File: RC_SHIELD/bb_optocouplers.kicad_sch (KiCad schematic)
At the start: 40 parts, among them U1 SFH6345, U2 SFH6345, U6 SFH6345, U8 SFH6345

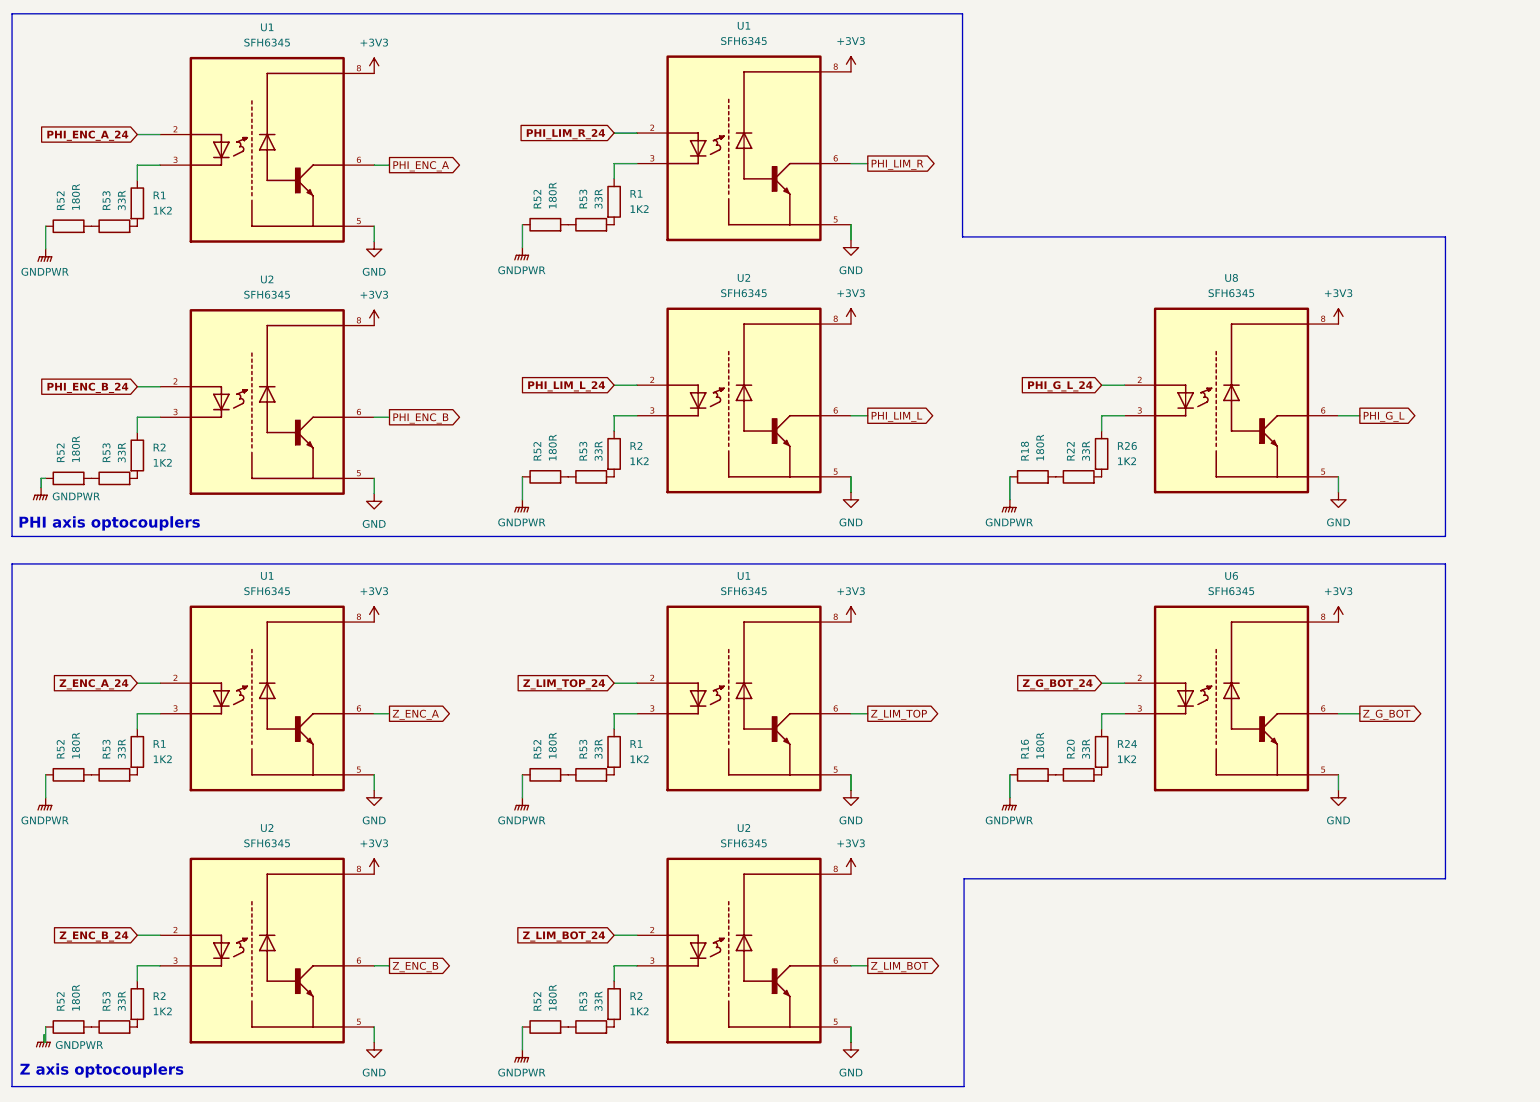
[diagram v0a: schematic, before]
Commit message: Revert "[SCH] reorganized optocouplers and tidied up page 2"
This reverts commit 005640e4067293c5014d1b79d289b32d97da3ff9.
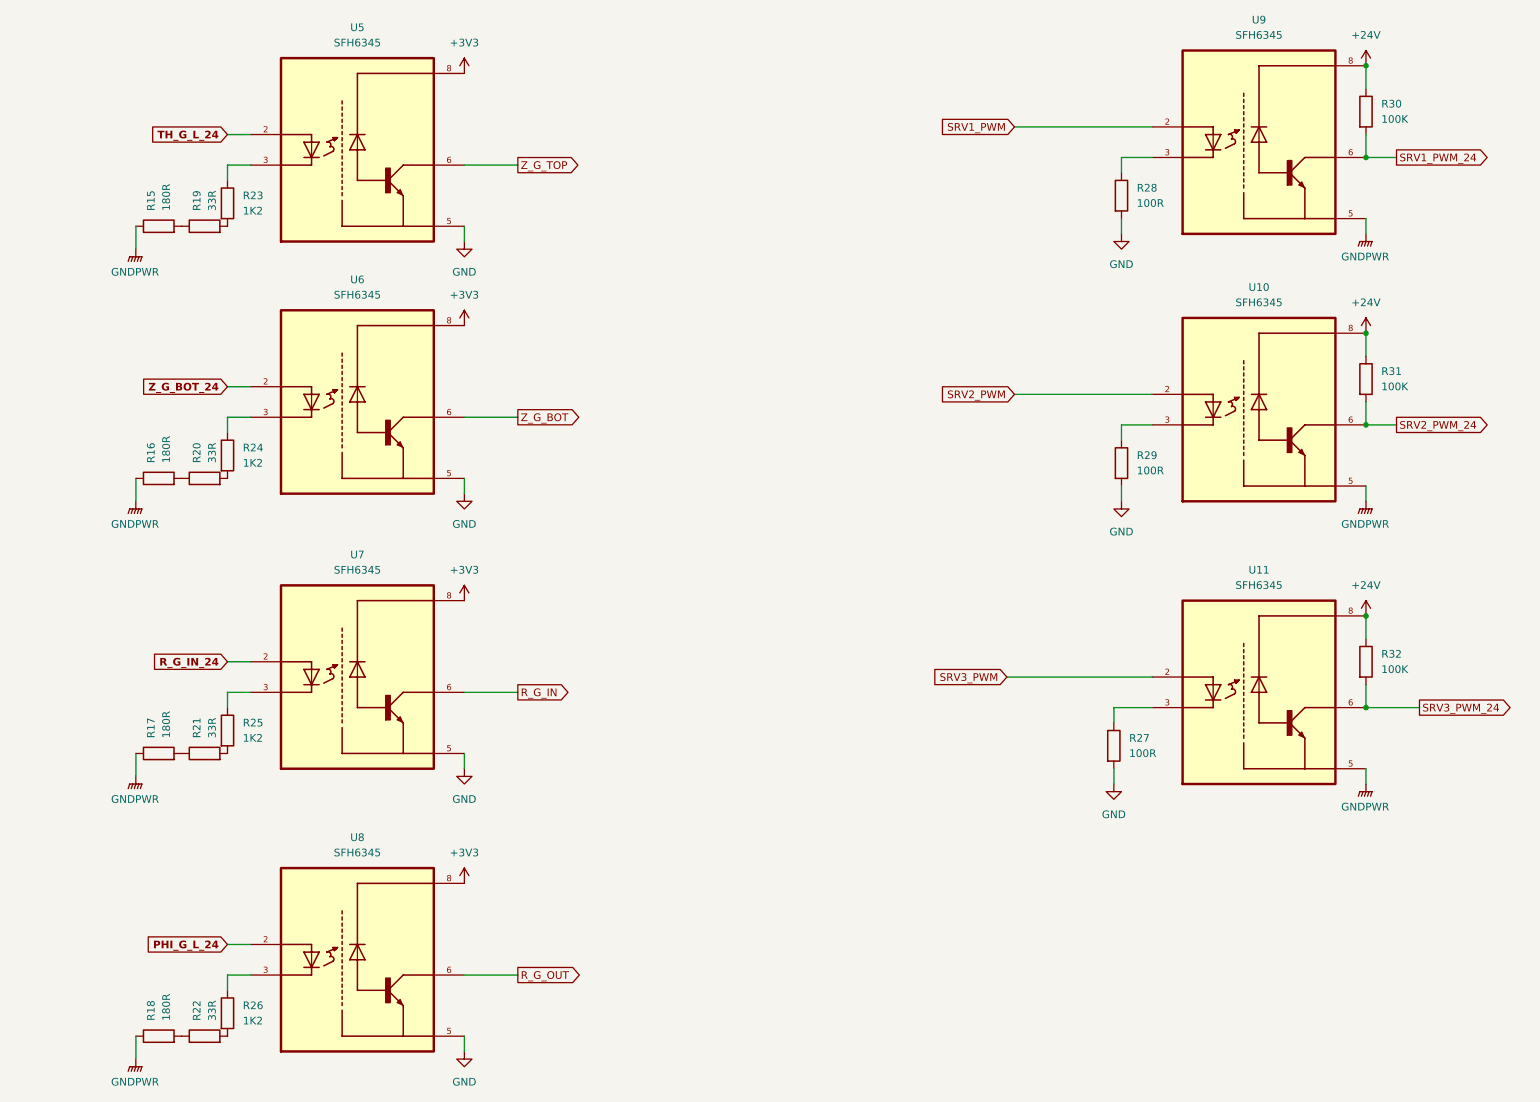
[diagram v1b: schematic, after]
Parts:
- removed R1 (x4), R2 (x4): 1K2, Resistor_SMD:R_0805_2012Metric_Pad1.20x1.40mm_HandSolder, symbol Device:R
- removed R52 (x8): 180R, Resistor_SMD:R_0805_2012Metric_Pad1.20x1.40mm_HandSolder, symbol Device:R
- removed R53 (x8): 33R, Resistor_SMD:R_0805_2012Metric_Pad1.20x1.40mm_HandSolder, symbol Device:R
- removed U1 (x4), U2 (x4): SFH6345, SFH6345:DIP762W50P254L977H451Q8, symbol SFH6345:SFH6345
- added R15, R17: 180R, Resistor_SMD:R_0805_2012Metric_Pad1.20x1.40mm_HandSolder, symbol Device:R
- added R19, R21: 33R, Resistor_SMD:R_0805_2012Metric_Pad1.20x1.40mm_HandSolder, symbol Device:R
- added R23, R25: 1K2, Resistor_SMD:R_0805_2012Metric_Pad1.20x1.40mm_HandSolder, symbol Device:R
- added R27, R28, R29: 100R, Resistor_SMD:R_0805_2012Metric_Pad1.20x1.40mm_HandSolder, symbol Device:R
- added R30, R31, R32: 100K, Resistor_SMD:R_0805_2012Metric_Pad1.20x1.40mm_HandSolder, symbol Device:R
- added U10, U11, U5, U7, U9: SFH6345, SFH6345:DIP762W50P254L977H451Q8, symbol SFH6345:SFH6345
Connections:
- net +3V3: now also U5.8, U7.8
- net GND: now also R27.2, R28.2, R29.2, U5.5, U7.5
- net GNDPWR: now also R15.1, R17.1, U10.5, U11.5, U9.5
- net PHI_G_L renamed R_G_OUT
- new net: R17.2, R21.1
- new net: R23.1, U5.3
- new net: R19.2, R23.2
- new net: R25.1, U7.3
- new net: R27.1, U11.3
- new net: R15.2, R19.1
- new net: R29.1, U10.3
- new net: R21.2, R25.2
- new net: R28.1, U9.3
- new net +24V: R30.1, R31.1, R32.1, U10.8, U11.8, U9.8
- new net R_G_IN: U7.6
- new net R_G_IN_24: U7.2
- new net SRV1_PWM: U9.2
- new net SRV1_PWM_24: R30.2, U9.6
- new net SRV2_PWM: U10.2
- new net SRV2_PWM_24: R31.2, U10.6
- new net SRV3_PWM: U11.2
- new net SRV3_PWM_24: R32.2, U11.6
- new net TH_G_L_24: U5.2
- new net Z_G_TOP: U5.6
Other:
- note removed: "PHI axis optocouplers"
- note removed: "Z axis optocouplers"
- title: Karcsi (INDACT Robot Arm) - Phi & Z axes optocouplers -> Karcsi (INDACT Robot Arm) - Servo & position-gate optocouplers
- moved on the sheet: R16, R18, R20, R22, R24, R26, U6, U8

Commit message: [SCH] fixed Nucleo papercuts
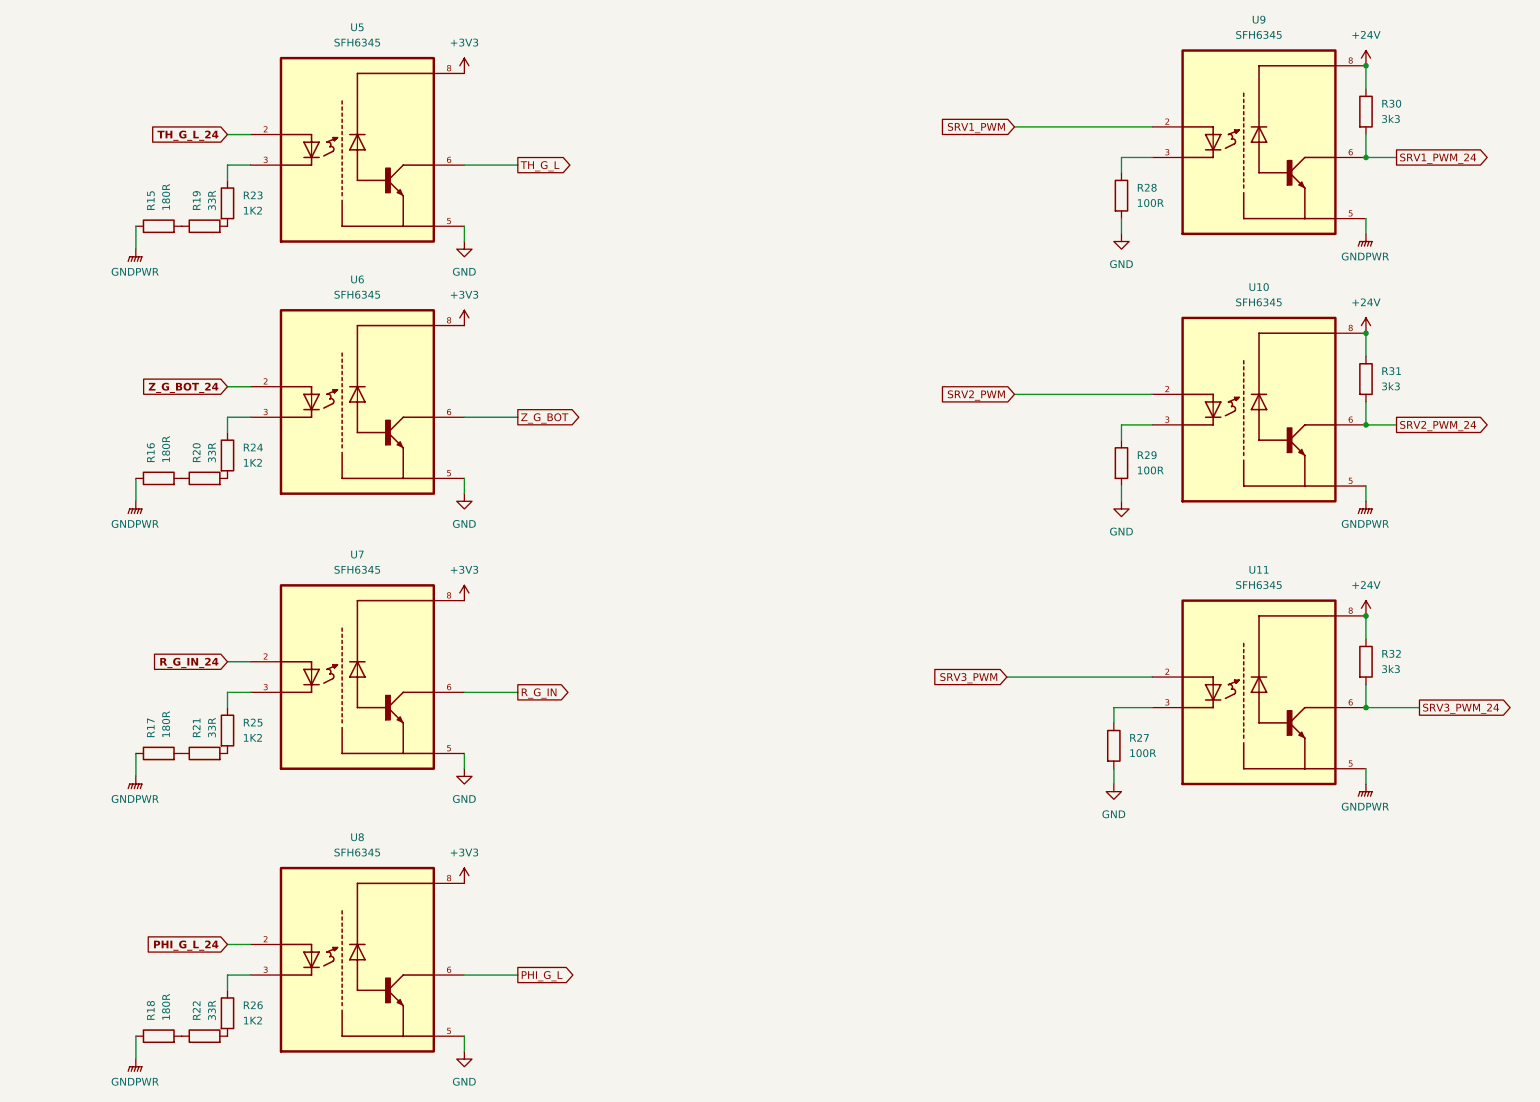
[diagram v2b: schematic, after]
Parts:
- R30, R31, R32: value 100K -> 3k3
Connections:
- net R_G_OUT renamed PHI_G_L
- net Z_G_TOP renamed TH_G_L
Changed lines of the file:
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@@
     )
   )
-  (global_label "R_G_OUT" (shape output) (at 100.33 175.26 0) (fields_autoplaced)
+  (global_label "PHI_G_L" (shape output) (at 100.33 175.26 0) (fields_autoplaced)
     (effects (font (size 1.27 1.27)) (justify left))
-    (property "Intersheetrefs" "${INTERSHEET_REFS}" (at 111.419 175.26 0)
+    (property "Intersheetrefs" "${INTERSHEET_REFS}" (at 110.7538 175.26 0)
       (effects (font (size 1.27 1.27)) (justify left))
     )
@@
     )
   )
-  (global_label "Z_G_TOP" (shape output) (at 100.33 40.64 0) (fields_autoplaced)
+  (global_label "TH_G_L" (shape output) (at 100.33 40.64 0) (fields_autoplaced)
     (effects (font (size 1.27 1.27)) (justify left))
-    (property "Intersheetrefs" "${INTERSHEET_REFS}" (at 111.298 40.64 0)
+    (property "Intersheetrefs" "${INTERSHEET_REFS}" (at 109.8466 40.64 0)
       (effects (font (size 1.27 1.27)) (justify left))
     )
@@
       (effects (font (size 1.27 1.27)) (justify left))
     )
-    (property "Value" "100K" (at 243.84 77.47 0)
+    (property "Value" "3k3" (at 243.84 77.47 0)
       (effects (font (size 1.27 1.27)) (justify left))
     )
@@
       (effects (font (size 1.27 1.27)) (justify left))
     )
-    (property "Value" "100K" (at 243.84 33.02 0)
+    (property "Value" "3k3" (at 243.84 33.02 0)
       (effects (font (size 1.27 1.27)) (justify left))
     )
@@
       (effects (font (size 1.27 1.27)) (justify left))
     )
-    (property "Value" "100K" (at 243.84 124.46 0)
-      (effects (font (size 1.27 1.27)) (justify left))
-    )
+    (property "Value" "3k3" (at 243.84 124.46 0)
+      (effects (font (size 1.27 1.27)) (justify left))
+    )
